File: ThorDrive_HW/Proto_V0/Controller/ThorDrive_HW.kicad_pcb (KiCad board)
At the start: 2 copper layers, 98.5 x 83.3 mm, 69 parts, among them J1 Conn_01x04_Socket, J10 Conn_01x03_Socket, J13 CTRL, J2 Conn_01x06_Socket, J3 Conn_01x03_Socket, J4 Conn_01x08_Socket, J5 Conn_01x08_Pin, J6 Conn_01x04_Pin, J7 Conn_01x06_Pin, J8 Conn_01x04_Pin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

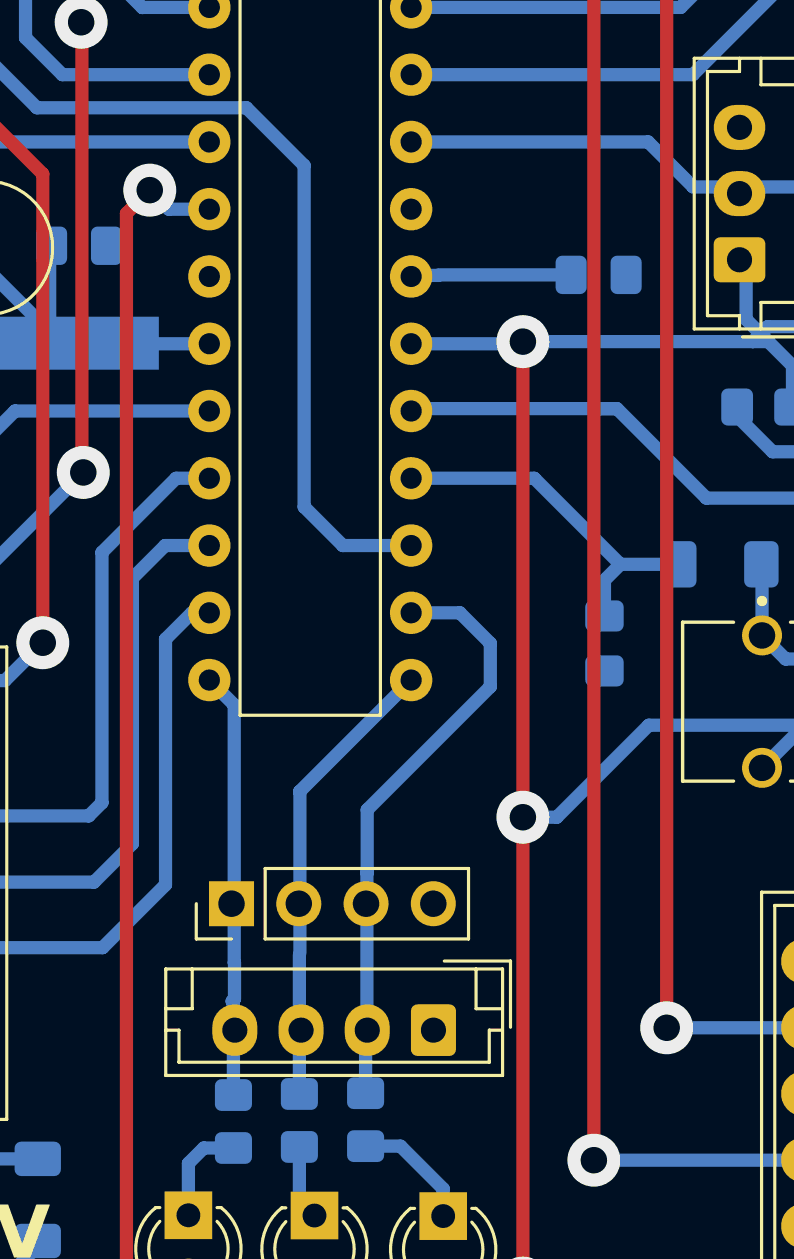
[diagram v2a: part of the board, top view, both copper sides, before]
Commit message: Added Basic Drivers, Initialized system manager
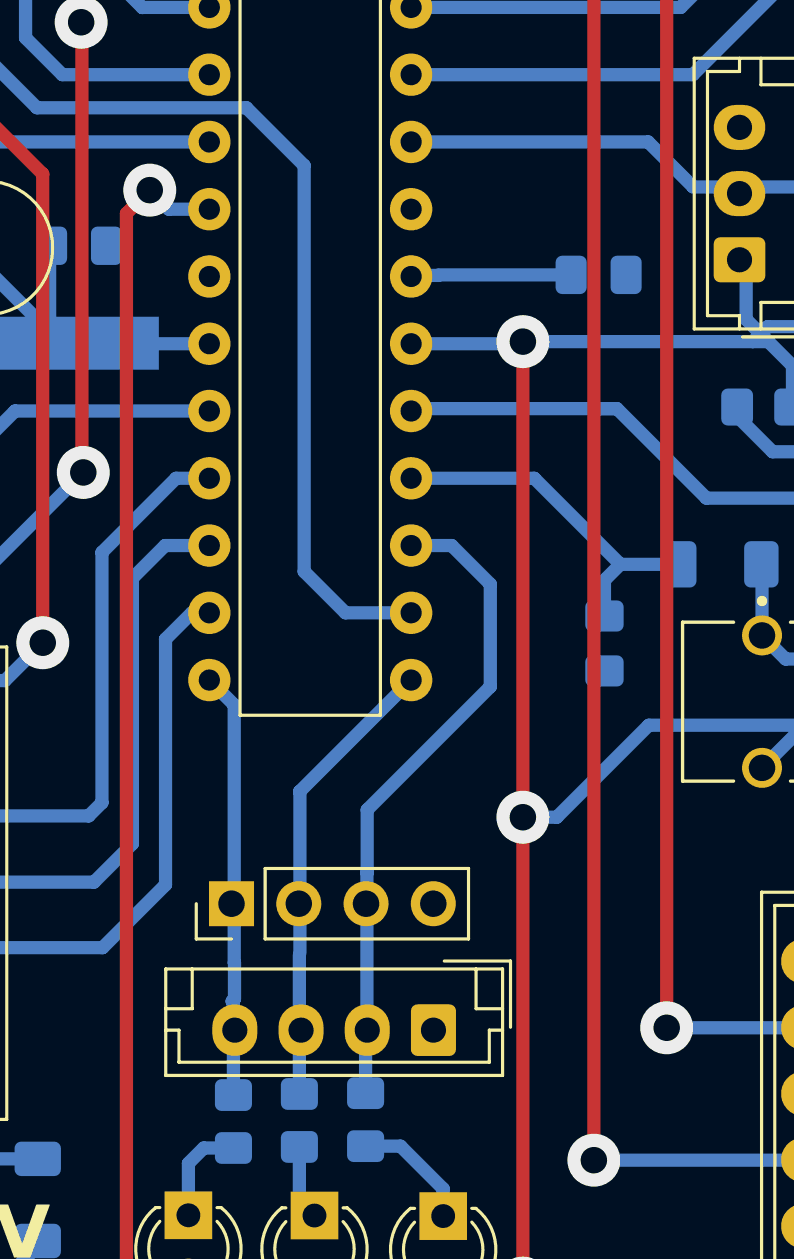
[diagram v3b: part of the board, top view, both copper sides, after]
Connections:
- U1 pad 16: HallC -> speed
- U1 pad 17: speed -> HallC
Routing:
- net speed: track 50.2 -> 52.7 mm
- net HallC: track 22.4 -> 24.8 mm
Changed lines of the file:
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@@
 			(layers "*.Cu" "*.Mask")
 			(remove_unused_layers no)
-			(net 11 "HallC")
+			(net 41 "speed")
 			(pinfunction "PB2")
 			(pintype "bidirectional")
@@
 			(layers "*.Cu" "*.Mask")
 			(remove_unused_layers no)
-			(net 41 "speed")
+			(net 11 "HallC")
 			(pinfunction "PB3")
 			(pintype "bidirectional")
@@
 	)
 	(segment
-		(start 69.9475 67.705)
-		(end 65.2975 72.355)
+		(start 65.2875 80.545)
+		(end 65.2375 80.595)
 		(width 0.5)
 		(layer "B.Cu")
@@
 	)
 	(segment
-		(start 66.9575 64.915)
-		(end 68.7975 64.915)
+		(start 68.4875 62.375)
+		(end 69.9475 63.835)
 		(width 0.5)
 		(layer "B.Cu")
@@
 	)
 	(segment
-		(start 65.2375 83.055)
-		(end 65.2375 80.595)
+		(start 65.2375 80.595)
+		(end 65.2375 83.055)
 		(width 0.5)
 		(layer "B.Cu")
@@
 	)
 	(segment
-		(start 65.2875 80.545)
-		(end 65.2375 80.595)
+		(start 66.9575 62.375)
+		(end 68.4875 62.375)
 		(width 0.5)
 		(layer "B.Cu")
@@
 	)
 	(segment
-		(start 69.9475 66.065)
-		(end 69.9475 67.705)
+		(start 65.2975 74.725)
+		(end 65.2875 74.735)
 		(width 0.5)
 		(layer "B.Cu")
@@
 	)
 	(segment
-		(start 65.2875 74.735)
-		(end 65.2875 80.545)
+		(start 69.9475 63.835)
+		(end 69.9475 67.705)
 		(width 0.5)
 		(layer "B.Cu")
@@
 	)
 	(segment
-		(start 65.2975 74.725)
-		(end 65.2875 74.735)
+		(start 65.2875 74.735)
+		(end 65.2875 80.545)
 		(width 0.5)
 		(layer "B.Cu")
@@
 	)
 	(segment
-		(start 68.7975 64.915)
-		(end 69.9475 66.065)
+		(start 69.9475 67.705)
+		(end 65.2975 72.355)
 		(width 0.5)
 		(layer "B.Cu")
@@
 	)
 	(segment
-		(start 48.3375 39.045)
-		(end 49.6175 40.325)
+		(start 49.6175 40.325)
+		(end 49.6175 40.335)
 		(width 0.5)
 		(layer "B.Cu")
@@
 	)
 	(segment
+		(start 62.9175 48.025)
+		(end 62.9175 63.355)
+		(width 0.5)
+		(layer "B.Cu")
+		(net 41)
+	)
+	(segment
 		(start 44.2875 35.235)
 		(end 43.6775 35.845)
@@
 	)
 	(segment
-		(start 43.6775 35.845)
-		(end 43.6875 35.855)
+		(start 52.8275 45.845)
+		(end 60.7375 45.845)
 		(width 0.5)
 		(layer "B.Cu")
@@
 	)
 	(segment
-		(start 43.6875 38.925)
-		(end 45.8375 38.925)
+		(start 43.6775 35.845)
+		(end 43.6875 35.855)
 		(width 0.5)
 		(layer "B.Cu")
@@
 	)
 	(segment
-		(start 49.6175 40.325)
-		(end 49.6175 40.335)
+		(start 43.6875 38.925)
+		(end 45.8375 38.925)
 		(width 0.5)
 		(layer "B.Cu")
@@
 	)
 	(segment
-		(start 62.9175 60.915)
-		(end 64.3775 62.375)
+		(start 41.1275 38.925)
+		(end 41.0075 39.045)
 		(width 0.5)
 		(layer "B.Cu")
@@
 	)
 	(segment
-		(start 41.1275 38.925)
-		(end 41.0075 39.045)
+		(start 64.4775 64.915)
+		(end 66.9575 64.915)
 		(width 0.5)
 		(layer "B.Cu")
@@
 	)
 	(segment
-		(start 52.8275 45.845)
-		(end 60.7375 45.845)
+		(start 50.3875 43.405)
+		(end 52.8275 45.845)
 		(width 0.5)
 		(layer "B.Cu")
@@
 	)
 	(segment
-		(start 64.3775 62.375)
-		(end 66.9575 62.375)
+		(start 60.7375 45.845)
+		(end 62.9175 48.025)
 		(width 0.5)
 		(layer "B.Cu")
@@
 	)
 	(segment
-		(start 62.9175 48.025)
-		(end 62.9175 60.915)
-		(width 0.5)
-		(layer "B.Cu")
-		(net 41)
-	)
-	(segment
 		(start 45.8375 38.925)
 		(end 45.9575 39.045)
@@
 	)
 	(segment
-		(start 60.7375 45.845)
-		(end 62.9175 48.025)
+		(start 62.9175 63.355)
+		(end 64.4775 64.915)
 		(width 0.5)
 		(layer "B.Cu")
@@
 	)
 	(segment
-		(start 50.3875 43.405)
-		(end 52.8275 45.845)
+		(start 48.3375 39.045)
+		(end 49.6175 40.325)
 		(width 0.5)
 		(layer "B.Cu")
